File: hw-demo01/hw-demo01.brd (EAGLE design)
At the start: 63.2 x 63.5 mm, 37 parts, among them IC3 MCP2562T, IC4 STM32F042

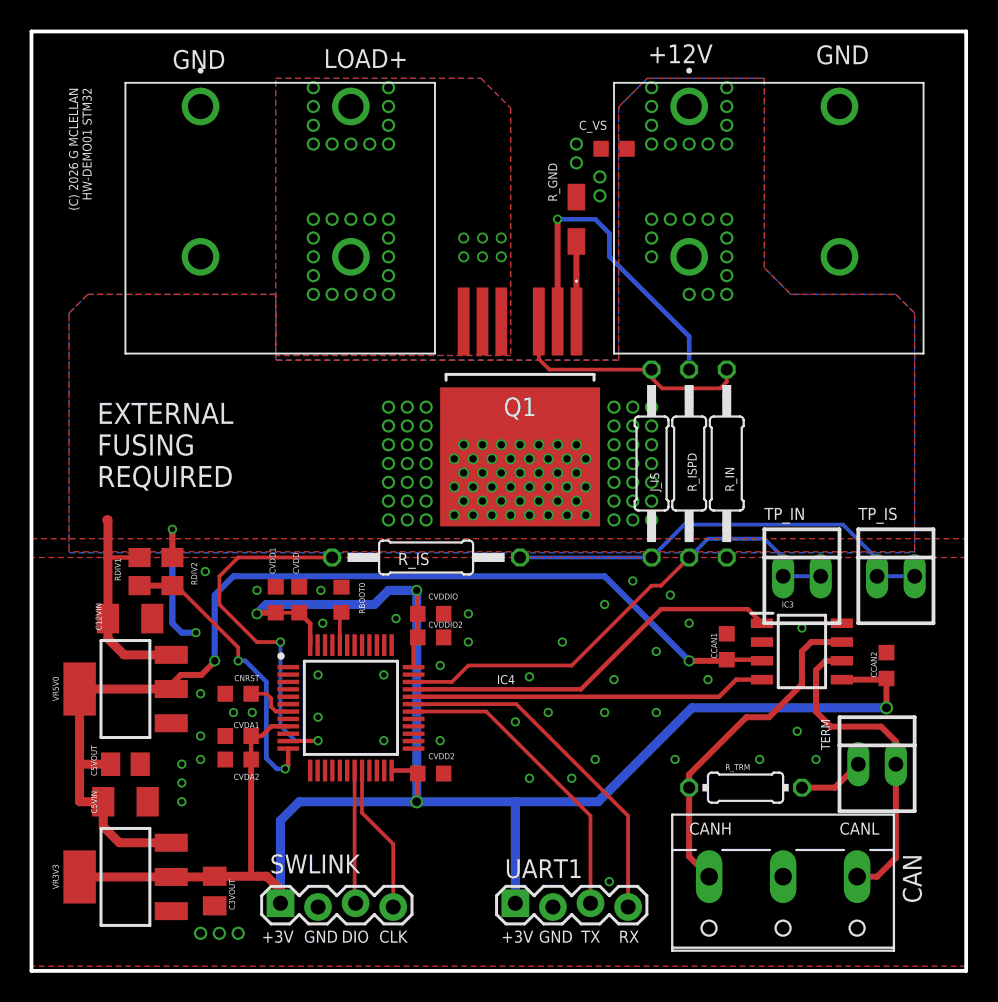
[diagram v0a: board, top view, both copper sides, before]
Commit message: added stitching based on review of reference designs
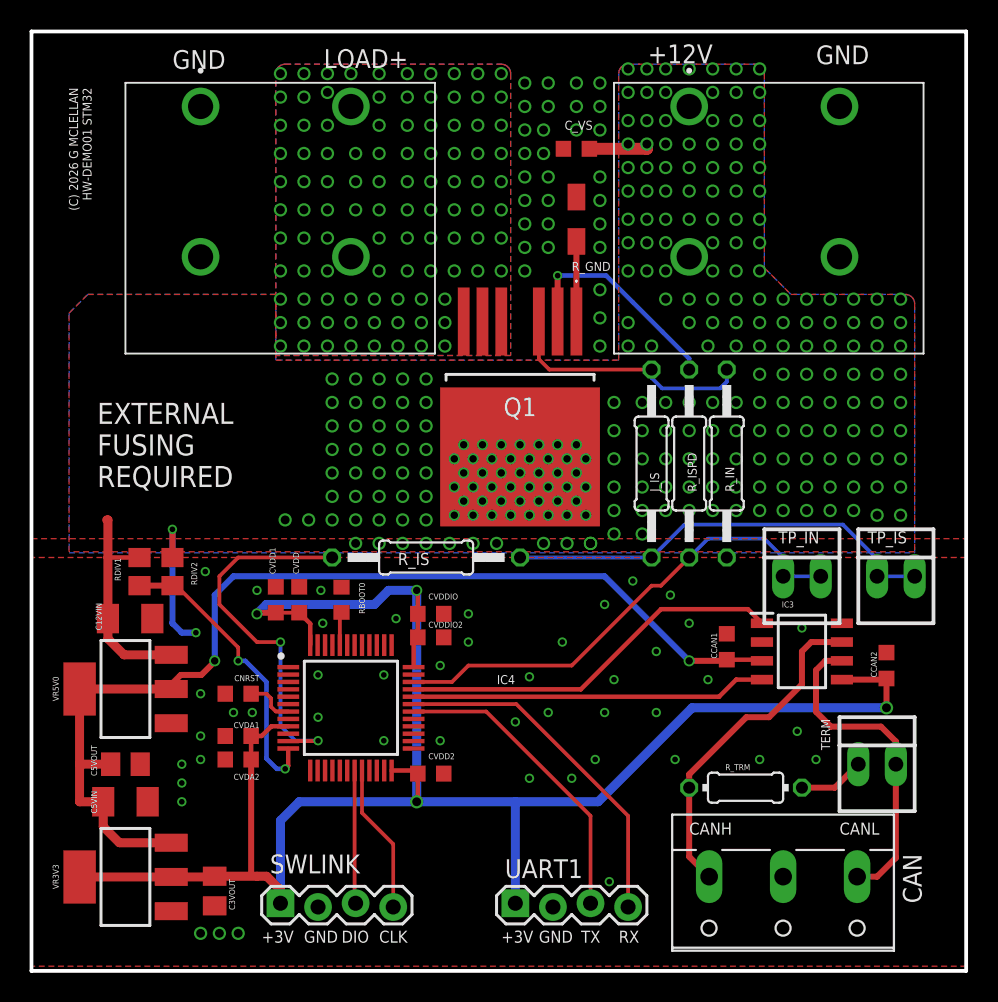
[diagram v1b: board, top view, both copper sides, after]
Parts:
- moved C_VS 2.54 mm to (38.1, 55.6)
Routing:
- net CTL3`: track 22.2 -> 15.1 mm
- net +12V: track 15.0 -> 19.2 mm, vias 111 -> 259
- net GND: vias 52 -> 78
